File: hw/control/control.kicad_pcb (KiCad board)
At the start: 2 copper layers, 200 x 100 mm, 128 parts, among them J101 Screw_Terminal_01x02, J102 Screw_Terminal_01x03, J103 Screw_Terminal_01x03, J301 Conn_02x05_Odd_Even, J302 Conn_01x04, J303 Raspberry_Pi_0_2_3, J304 Micro_SD_Card, J305 Conn_01x06, Q1001 BC807, Q1002 BC817, Q401 BC817, Q501 BC817, Q601 BC817, Q701 BC817, Q801 BC807, Q802 BC817, Q901 AOSP21357, U1001 LM2678T-ADJ, U1101 SN74AHCT125D, U201 LM2596T-ADJ, U801 LM2678T-ADJ

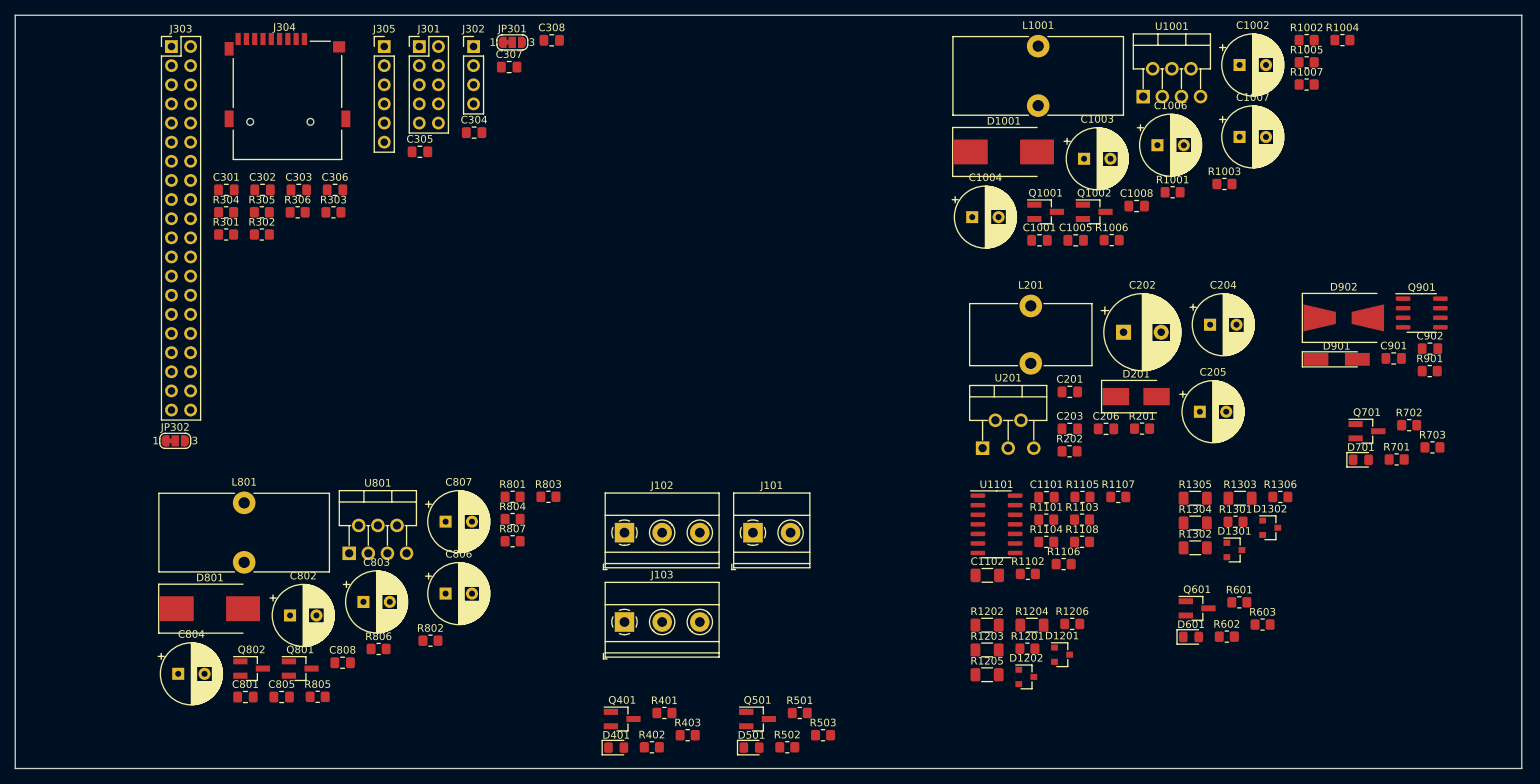
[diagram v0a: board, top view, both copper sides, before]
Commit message: [hw] Spread-out the components on control layout
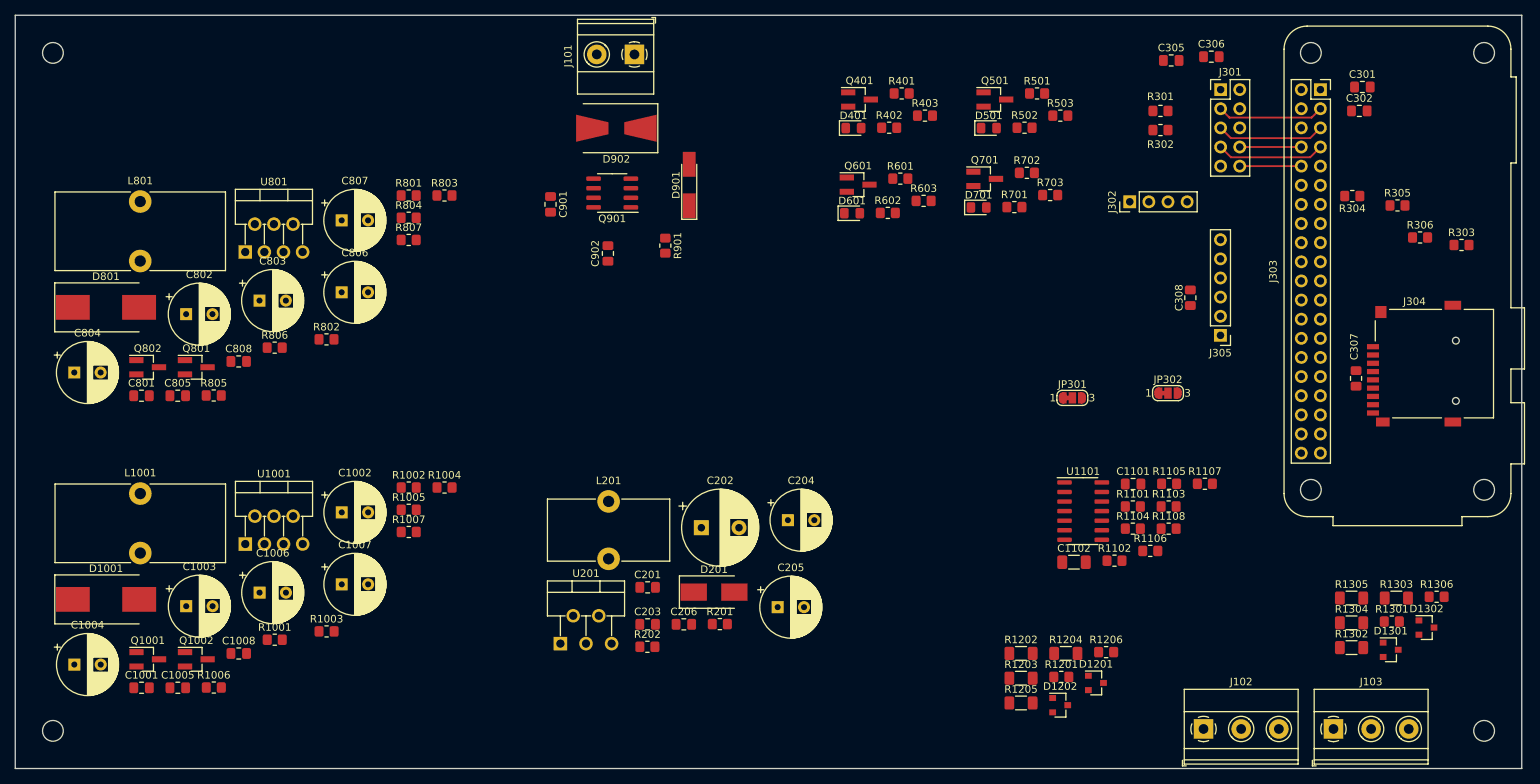
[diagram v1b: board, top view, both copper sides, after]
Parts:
- removed C303, C304: 100n, Capacitor_SMD:C_0805_2012Metric_Pad1.18x1.45mm_HandSolder
- added H101: MountingHole, MountingHole:MountingHole_2.7mm_M2.5, F.Cu at (238.5, 149.7)
- added H102: MountingHole, MountingHole:MountingHole_2.7mm_M2.5, F.Cu at (48.5, 149.7)
- added H103: MountingHole, MountingHole:MountingHole_2.7mm_M2.5, F.Cu at (48.5, 59.7)
- J303: footprint Connector_PinHeader_2.54mm:PinHeader_2x20_P2.54mm_Vertical -> Module:Raspberry_Pi_Zero_Socketed_THT_FaceDown_MountingHoles
- moved J304 158.4 mm to (234.8, 101.0), turned to 90 degrees
- moved J303 152.6 mm to (216.8, 64.6)
- moved C301 151.4 mm to (222.3, 64.2)
- moved R305 150.8 mm to (227.0, 80.0)
- moved R303 149.8 mm to (235.5, 85.2)
- moved R304 149.5 mm to (221.0, 78.7), turned to 180 degrees
- moved R306 149.0 mm to (230.0, 84.2)
- moved C302 146.0 mm to (221.9, 67.4)
- moved C1002 133.2 mm to (86.8, 120.7)
- moved C1004 133.2 mm to (51.3, 140.9)
- moved C1007 133.2 mm to (86.8, 130.2)
- moved L1001 133.2 mm to (60.1, 118.2)
- moved C1001 133.2 mm to (60.3, 144.0)
- moved C1003 133.2 mm to (66.2, 133.2)
- moved C1005 133.2 mm to (65.1, 144.0)
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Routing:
- net /CPU/IIC0_SCL: track 0.00 -> 14.4 mm
- net /CPU/GPIO4: track 0.00 -> 14.4 mm
- net /CPU/IIC0_SDA: track 0.00 -> 14.2 mm
- net /CPU/UART_TXD: track 0.00 -> 8.17 mm
- net /CPU/UART_RXD: track 0.00 -> 8.17 mm

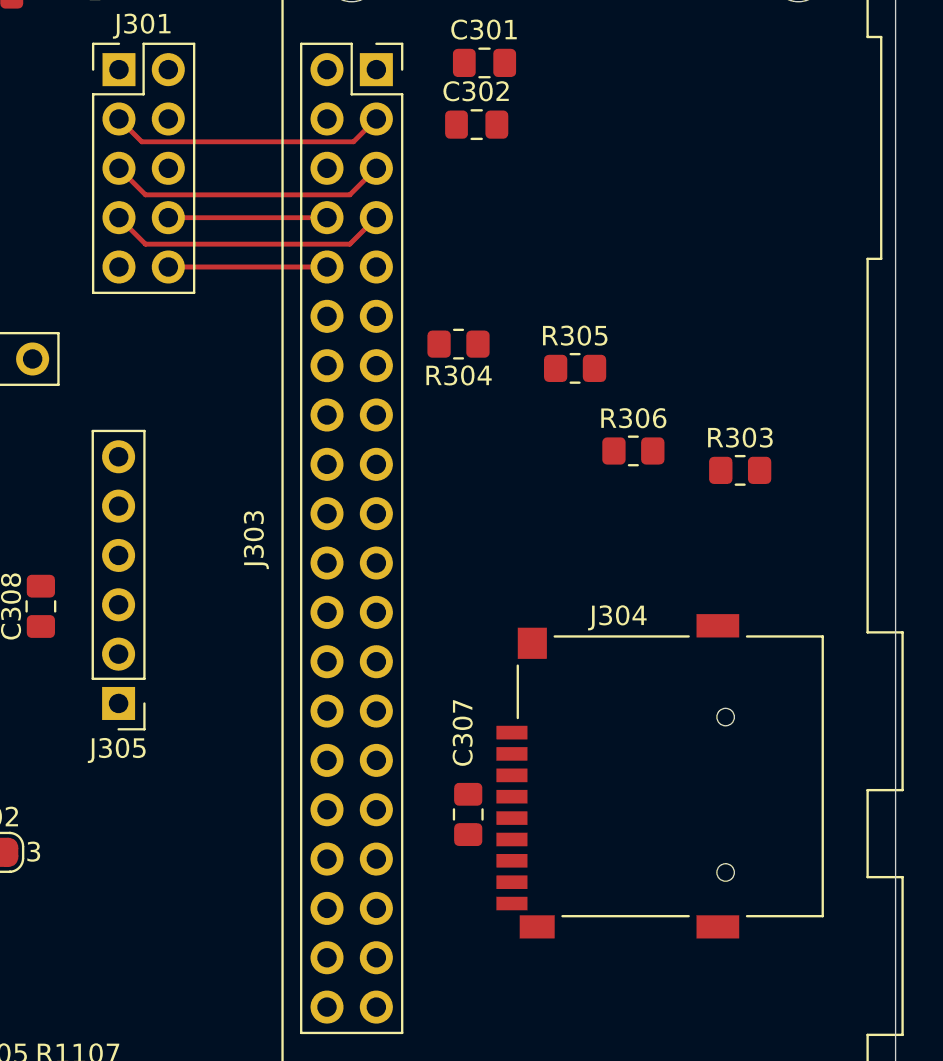
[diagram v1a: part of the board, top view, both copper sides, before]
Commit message: [hw] Add control board net classes
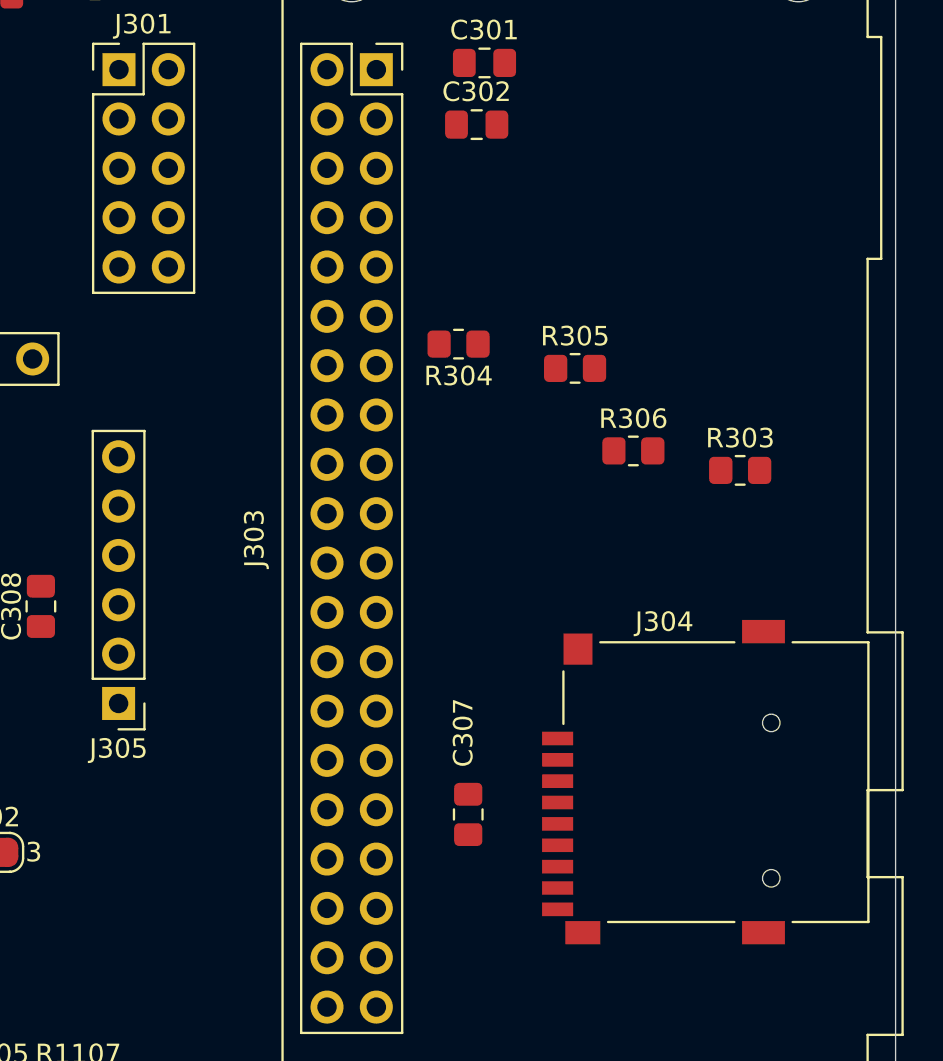
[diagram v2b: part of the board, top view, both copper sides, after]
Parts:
- J303: footprint Module:Raspberry_Pi_Zero_Socketed_THT_FaceDown_MountingHoles -> my:Raspberry_Pi_Zero_Socketed_THT_FaceDown_MountingHoles_No_Courtyard
- moved J304 2.37 mm to (237.1, 101.2)
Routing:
- net /CPU/IIC0_SCL: track 14.4 -> 0.00 mm
- net /CPU/GPIO4: track 14.4 -> 0.00 mm
- net /CPU/IIC0_SDA: track 14.2 -> 0.00 mm
- net /CPU/UART_TXD: track 8.17 -> 0.00 mm
- net /CPU/UART_RXD: track 8.17 -> 0.00 mm
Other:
- net class Driver Signal added: clearance 0.5, trace_width 0.35, via_dia 0.8, via_drill 0.4
- net class Power added: clearance 0.2, trace_width 1, via_dia 0.8, via_drill 0.4
- net class Raw Power added: clearance 0.5, trace_width 0.25, via_dia 0.8, via_drill 0.4
- net class Signal added: clearance 0.2, trace_width 0.25, via_dia 0.8, via_drill 0.4

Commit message: [hw] Incorporate suggestions
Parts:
- added Q902: IRF9540N, Package_TO_SOT_THT:TO-220-3_Vertical, F.Cu at (135.1, 67.7)
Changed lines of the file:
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@@
     (tracks 0)
     (zones 0)
-    (modules 129)
+    (modules 130)
     (nets 80)
   )
@@
     (add_net "Net-(J302-Pad2)")
     (add_net "Net-(J302-Pad3)")
+    (add_net "Net-(J303-Pad27)")
+    (add_net "Net-(J303-Pad28)")
+    (add_net "Net-(J303-Pad29)")
+    (add_net "Net-(J303-Pad31)")
     (add_net "Net-(J303-Pad32)")
     (add_net "Net-(J303-Pad33)")
+    (add_net "Net-(J303-Pad35)")
+    (add_net "Net-(J303-Pad36)")
+    (add_net "Net-(J303-Pad40)")
+    (add_net "Net-(J304-Pad1)")
     (add_net "Net-(J304-Pad2)")
     (add_net "Net-(J304-Pad3)")
     (add_net "Net-(J304-Pad5)")
     (add_net "Net-(J304-Pad7)")
+    (add_net "Net-(J304-Pad8)")
     (add_net "Net-(Q1001-Pad1)")
     (add_net "Net-(Q1002-Pad1)")
@@
     (add_net "Net-(R1104-Pad1)")
     (add_net "Net-(R801-Pad1)")
+    (add_net "Net-(U1001-Pad5)")
+    (add_net "Net-(U801-Pad5)")
   )
   (net_class "Driver Signal" ""
@@
     (add_net /LED_PWR_EN1)
   )
+  (module Package_TO_SOT_THT:TO-220-3_Vertical (layer F.Cu)
+    (at 135.1 67.7)
+    (descr "TO-220-3, Vertical, RM 2.54mm, see https://www.vishay.com/docs/66542/to-220-1.pdf")
+    (tags "TO-220-3 Vertical RM 2.54mm")
+    (fp_text reference Q902 (at 2.54 -4.27) (layer F.SilkS)
+      (effects (font (size 1 1) (thickness 0.15)))
+    )
+    (fp_text value IRF9540N (at 2.54 2.5) (layer F.Fab)
+      (effects (font (size 1 1) (thickness 0.15)))
+    )
+    (fp_line (start 7.79 -3.4) (end -2.71 -3.4) (layer F.CrtYd) (width 0.05))
+    (fp_line (start 7.79 1.51) (end 7.79 -3.4) (layer F.CrtYd) (width 0.05))
+    (fp_line (start -2.71 1.51) (end 7.79 1.51) (layer F.CrtYd) (width 0.05))
+    (fp_line (start -2.71 -3.4) (end -2.71 1.51) (layer F.CrtYd) (width 0.05))
+    (fp_line (start 4.391 -3.27) (end 4.391 -1.76) (layer F.SilkS) (width 0.12))
+    (fp_line (start 0.69 -3.27) (end 0.69 -1.76) (layer F.SilkS) (width 0.12))
+    (fp_line (start -2.58 -1.76) (end 7.66 -1.76) (layer F.SilkS) (width 0.12))
+    (fp_line (start 7.66 -3.27) (end 7.66 1.371) (layer F.SilkS) (width 0.12))
+    (fp_line (start -2.58 -3.27) (end -2.58 1.371) (layer F.SilkS) (width 0.12))
+    (fp_line (start -2.58 1.371) (end 7.66 1.371) (layer F.SilkS) (width 0.12))
+    (fp_line (start -2.58 -3.27) (end 7.66 -3.27) (layer F.SilkS) (width 0.12))
+    (fp_line (start 4.39 -3.15) (end 4.39 -1.88) (layer F.Fab) (width 0.1))
+    (fp_line (start 0.69 -3.15) (end 0.69 -1.88) (layer F.Fab) (width 0.1))
+    (fp_line (start -2.46 -1.88) (end 7.54 -1.88) (layer F.Fab) (width 0.1))
+    (fp_line (start 7.54 -3.15) (end -2.46 -3.15) (layer F.Fab) (width 0.1))
+    (fp_line (start 7.54 1.25) (end 7.54 -3.15) (layer F.Fab) (width 0.1))
+    (fp_line (start -2.46 1.25) (end 7.54 1.25) (layer F.Fab) (width 0.1))
+    (fp_line (start -2.46 -3.15) (end -2.46 1.25) (layer F.Fab) (width 0.1))
+    (fp_text user %R (at 2.54 -4.27) (layer F.Fab)
+      (effects (font (size 1 1) (thickness 0.15)))
+    )
+    (pad 3 thru_hole oval (at 5.08 0) (size 1.905 2) (drill 1.1) (layers *.Cu *.Mask)
+      (net 4 "/LED0 Power/VIN"))
+    (pad 2 thru_hole oval (at 2.54 0) (size 1.905 2) (drill 1.1) (layers *.Cu *.Mask)
+      (net 9 "/Input Protection/V_A"))
+    (pad 1 thru_hole rect (at 0 0) (size 1.905 2) (drill 1.1) (layers *.Cu *.Mask)
+      (net 18 "Net-(D901-Pad2)"))
+    (model ${KISYS3DMOD}/Package_TO_SOT_THT.3dshapes/TO-220-3_Vertical.wrl
+      (at (xyz 0 0 0))
+      (scale (xyz 1 1 1))
+      (rotate (xyz 0 0 0))
+    )
+  )
   (module my:Raspberry_Pi_Zero_Socketed_THT_FaceDown_MountingHoles_No_Courtyard (layer F.Cu)
     (at 216.77 64.57)
@@
     )
     (fp_text value Raspberry_Pi_0_2_3 (at 10.23 24.13 270) (layer F.Fab)
-      (effects (font (size 1 1) (thickness 0.15)))
-    )
-    (fp_arc (start 22.23 -5.37) (end 22.23 -8.43) (angle 90) (layer F.SilkS) (width 0.12))
-    (fp_arc (start 22.23 53.63) (end 25.23 53.63) (angle 90) (layer F.Fab) (width 0.1))
-    (fp_arc (start -1.77 -5.37) (end -4.83 -5.37) (angle 90) (layer F.SilkS) (width 0.12))
-    (fp_arc (start -1.77 53.63) (end -1.77 56.69) (angle 90) (layer F.SilkS) (width 0.12))
-    (fp_arc (start 22.23 53.63) (end 25.29 53.63) (angle 90) (layer F.SilkS) (width 0.12))
-    (fp_arc (start 22.23 -5.37) (end 22.23 -8.37) (angle 90) (layer F.Fab) (width 0.1))
-    (fp_arc (start -1.77 -5.37) (end -4.77 -5.37) (angle 90) (layer F.Fab) (width 0.1))
-    (fp_arc (start -1.77 53.63) (end -1.77 56.63) (angle 90) (layer F.Fab) (width 0.1))
-    (fp_text user %R (at -1.27 24.13 90) (layer F.Fab)
       (effects (font (size 1 1) (thickness 0.15)))
     )
@@
     (fp_line (start 27.03 49.63) (end 27.03 41.63) (layer F.Fab) (width 0.1))
     (fp_line (start 27.03 41.63) (end 25.23 41.63) (layer F.Fab) (width 0.1))
+    (fp_arc (start 22.23 -5.37) (end 22.23 -8.43) (angle 90) (layer F.SilkS) (width 0.12))
+    (fp_arc (start 22.23 53.63) (end 25.23 53.63) (angle 90) (layer F.Fab) (width 0.1))
+    (fp_arc (start -1.77 -5.37) (end -4.83 -5.37) (angle 90) (layer F.SilkS) (width 0.12))
+    (fp_arc (start -1.77 53.63) (end -1.77 56.69) (angle 90) (layer F.SilkS) (width 0.12))
+    (fp_arc (start 22.23 53.63) (end 25.29 53.63) (angle 90) (layer F.SilkS) (width 0.12))
+    (fp_arc (start 22.23 -5.37) (end 22.23 -8.37) (angle 90) (layer F.Fab) (width 0.1))
+    (fp_arc (start -1.77 -5.37) (end -4.77 -5.37) (angle 90) (layer F.Fab) (width 0.1))
+    (fp_arc (start -1.77 53.63) (end -1.77 56.63) (angle 90) (layer F.Fab) (width 0.1))
+    (fp_text user %R (at -1.27 24.13 90) (layer F.Fab)
+      (effects (font (size 1 1) (thickness 0.15)))
+    )
     (pad 6 thru_hole oval (at -2.54 5.08) (size 1.7 1.7) (drill 1) (layers *.Cu *.Mask)
       (net 3 GND))
